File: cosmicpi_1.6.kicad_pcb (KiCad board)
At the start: 4 copper layers, 129.5 x 184 mm, 230 parts, among them J1 Barrel_Jack_Switch, J10 Conn_01x02_Female, J11 Conn_01x02_Male, J12 Conn_01x02_Male, J13 Conn_01x02_Female, J14 Conn_01x02_Male, J15 Conn_01x02_Female, J2 SMA, J3 USB_B_Micro, J4 Conn_01x04_Male, J5 Conn_01x04_Male, J6 SWD, J7 Raspberry_Pi_2_3, J8 Conn_01x02_Male, J9 Conn_01x02_Female, Q1 BSS123, Q2 BSS123, U1 MCP47CMB22, U10 TPS62163DSG, U11 LM555, U12 LM555, U13 LP2985-3.3, U14 AD8039, U15 AD8039, U16 LP2985-3.3, U17 MAX1932, U18 MAX1932, U19 AD8039, U2 STM32F401RETx, U3 L76-M33, U4 74HC00, U5 LPS25HB, U6 LM555, U7 LSM9DS1, U8 SI7006-A20, U9 MAX991, Y1 8 MHz

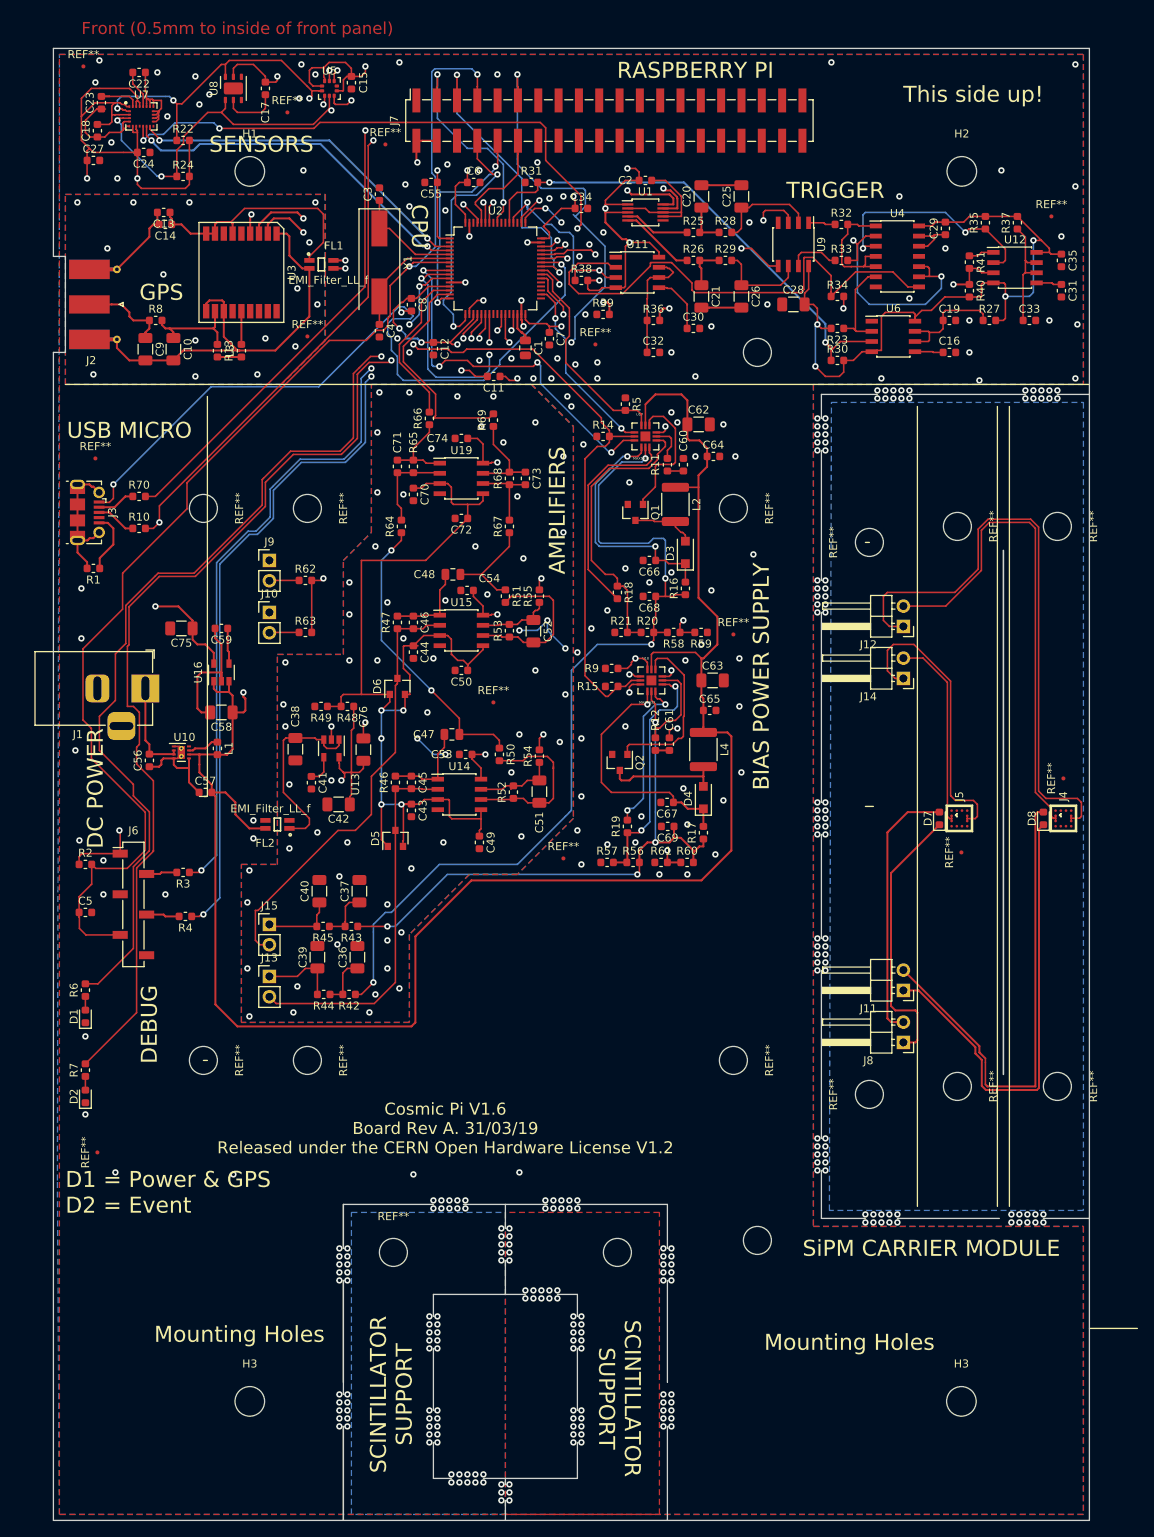
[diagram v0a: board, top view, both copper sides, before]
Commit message: Updated board size to fit in housing
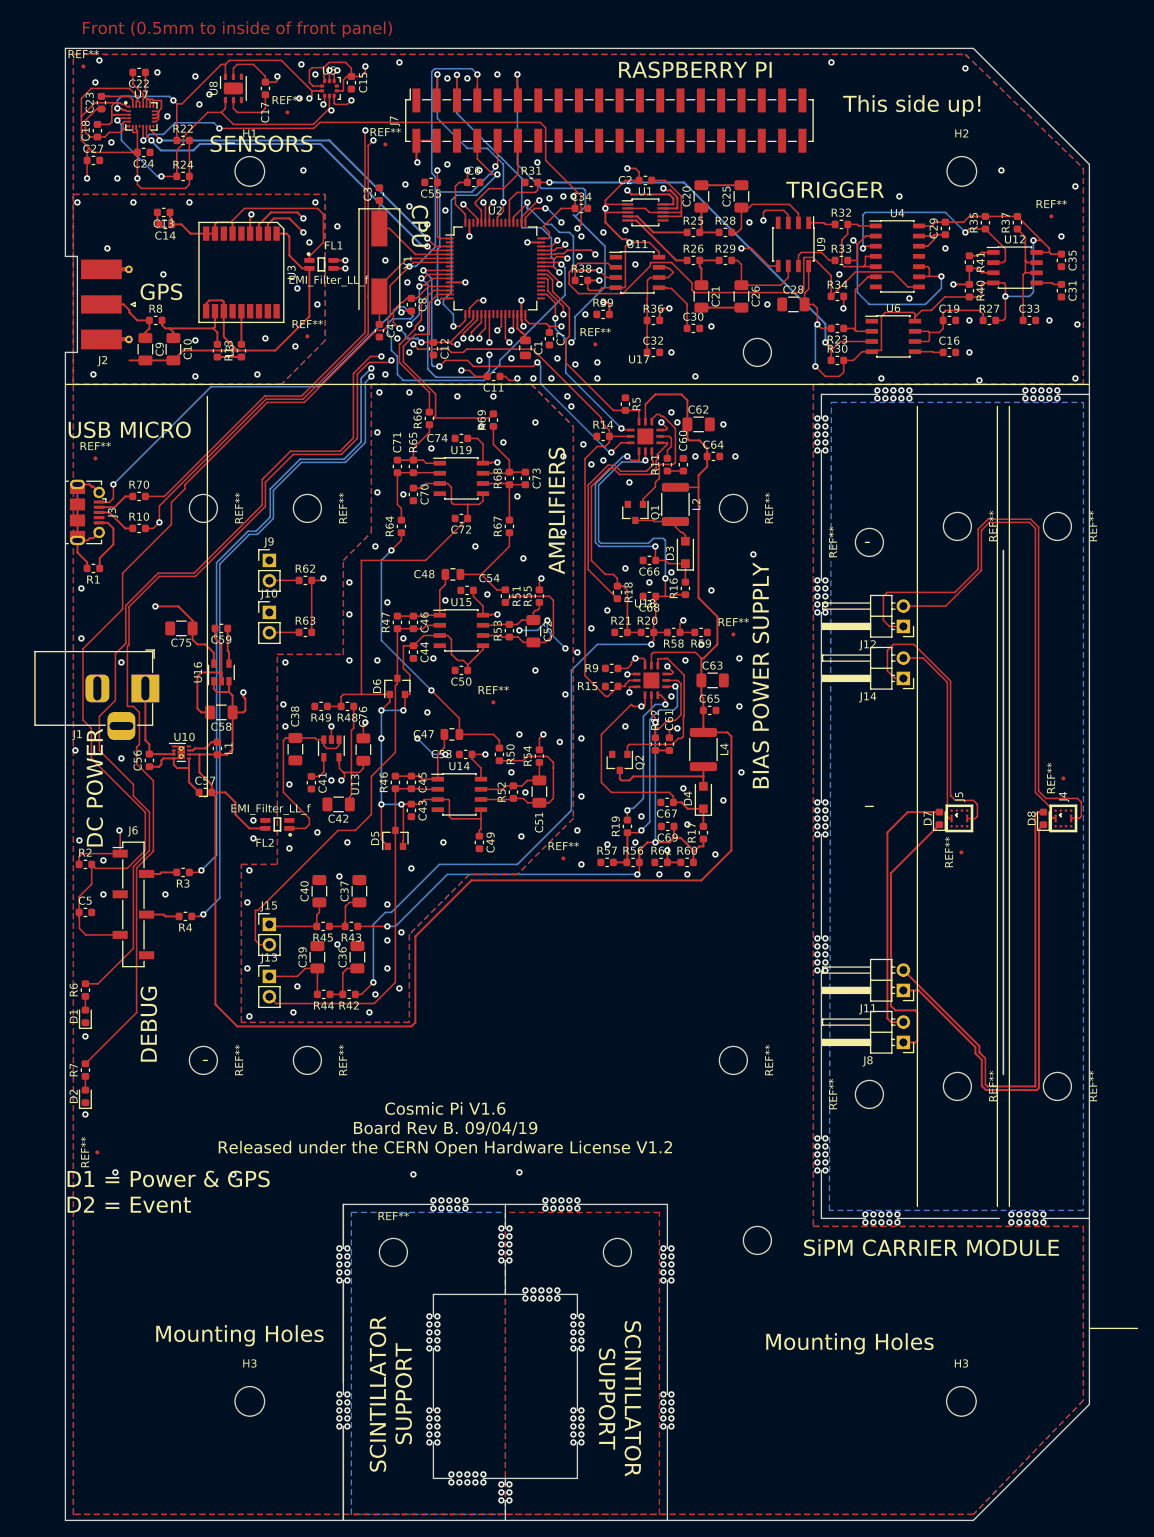
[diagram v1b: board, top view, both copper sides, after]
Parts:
- U17, U18: footprint MAX3806GTCT:21-0136I_T1233-3 -> maximsmd:QFN-12-1EP_4x4mm_P0.8mm
- moved J2 1.50 mm to (22.7, 50.0)
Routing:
- net GNDD: track 65.0 -> 53.5 mm
- net USB_OTG_DP: track 100.6 -> 111.1 mm
- net USB_OTG_DM: track 107.8 -> 111.5 mm
- net Net-(C9-Pad1): track 11.0 -> 12.2 mm
- net SHAPED_OUT_2: track 28.3 -> 29.3 mm
- net Net-(R18-Pad1): track 36.3 -> 37.2 mm
- net +5V: track 336.6 -> 335.7 mm
- net HVPSU_DIN: track 86.3 -> 85.5 mm
- net GND: track 138.5 -> 139.2 mm, vias 120 -> 136
- net Net-(Q1-Pad1): track 17.1 -> 16.4 mm
- net Net-(Q2-Pad1): track 21.9 -> 21.3 mm
- net Net-(R18-Pad2): track 26.6 -> 27.3 mm
- net HVPSU_CL2: track 83.4 -> 82.8 mm
- net HVPSU_CL1: track 48.4 -> 47.8 mm
- net Net-(R19-Pad1): track 30.0 -> 29.5 mm
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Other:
- board size 129.5 x 184 mm -> 128 x 184 mm
- board text added: "Cosmic Pi V1.6 Board Rev B. 09/04/19 Released under the CERN Open Hardware License V1.2"
- board text removed: "Cosmic Pi V1.6 Board Rev A. 31/03/19 Released under the CERN Open Hardware License V1.2"

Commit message: Incorporated comments from TE-MPE
They kindly checked the layout and schematic over for us! Can't be sure we got all the bugs until we build it though. Reversed raspberry pi header so that the connection will be inside the enclosure.
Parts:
- moved C15 1.75 mm to (54.0, 22.3)
- moved J7 0.57 mm to (83.9, 27.0), turned to 270 degrees
- moved C9 0.50 mm to (27.0, 55.6)
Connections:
- U2 pad 2: BARO_INT3 -> BARO_INT
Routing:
- net RX0: track 32.0 -> 83.2 mm
- net TX0: track 27.6 -> 78.7 mm
- net +5V: track 335.7 -> 373.2 mm, vias 2 -> 4
- net BARO_INT: track 0.00 -> 30.5 mm, vias 0 -> 2
- net BOOT0: track 13.8 -> 40.2 mm, vias 0 -> 2
- net _RESET: track 159.3 -> 178.8 mm
- net SDA_SLAVE: track 27.0 -> 43.2 mm
- net FLAG: track 59.0 -> 48.0 mm
- net GNDD: track 53.5 -> 48.0 mm
- net Net-(J12-Pad2): track 62.2 -> 57.3 mm
- net Net-(J12-Pad1): track 75.2 -> 70.5 mm
- net Net-(D8-Pad1): track 57.7 -> 60.0 mm
- net Net-(D8-Pad2): track 60.0 -> 62.3 mm
- net +3V3: track 305.6 -> 306.3 mm
- net SCL_SLAVE: track 37.2 -> 36.5 mm
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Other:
- outline, holes or cut-outs redrawn
- board text added: "Cosmic Pi V1.6 Board Rev C. 14/04/19 Released under the CERN Open Hardware License V1.2 cosmicpi.org"
- board text removed: "Cosmic Pi V1.6 Board Rev B. 09/04/19 Released under the CERN Open Hardware License V1.2"
